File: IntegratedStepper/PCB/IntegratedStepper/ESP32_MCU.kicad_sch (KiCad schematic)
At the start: 0 parts

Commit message: Update Integrated Stepper PCB with ESP sch and CAN sch
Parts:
- added C12, C19: 10uF, Capacitor_SMD:C_0603_1608Metric, symbol Device:C
- added C13, C14, C18: 0.1uF, Capacitor_SMD:C_0603_1608Metric, symbol Device:C
- added Q1, Q2: SS8050-G, SOT95P240X115-3N, symbol SamacSys_Parts:SS8050-G
- added R10: 22.1k, Resistor_SMD:R_0603_1608Metric, symbol Device:R_US
- added R11: 10, Resistor_SMD:R_0603_1608Metric, symbol Device:R_US
- added R12, R15, R16, R17, R18: 2k, Resistor_SMD:R_0603_1608Metric, symbol Device:R_US
- added R13, R14, R6: 10k, Resistor_SMD:R_0603_1608Metric, symbol Device:R_US
- added R9: 47.5k, Resistor_SMD:R_0603_1608Metric, symbol Device:R_US
- added U1: ESP32-WROOM-32E, RF_Module:ESP32-WROOM-32D, symbol RF_Module:ESP32-WROOM-32E
- added U3: CP2102N-Axx-xQFN28, Package_DFN_QFN:QFN-28-1EP_5x5mm_P0.5mm_EP3.35x3.35mm, symbol Interface_USB:CP2102N-Axx-xQFN28
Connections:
- new net: R12.1, U3.9 (~{RST})
- new net: Q2.1 (B), R14.2
- new net: R10.1, R9.1, U3.8 (VBUS)
- new net: Q1.1 (B), R13.2
- new net: R11.2, U1.35 (TXD0/IO1)
- new net 3V3_VCC: C12.1, C13.1, C18.1, C19.1, R12.2, R15.2, R17.1, R18.1, R6.1, U1.2 (VDD), U3.6 (VDD), U3.7 (VREGIN)
- new net CAN_RX: U1.28 (IO17)
- new net CAN_TX: U1.27 (IO16)
- new net DTR: Q2.2 (E), R13.1, U3.28 (~{DTR})
- new net EN: C14.1, Q1.3 (C), R6.2, U1.3 (EN)
- new net EN1: R17.2, U1.31 (IO19)
- new net EN3: R18.2, U1.37 (IO23)
- new net GND: C12.2, C13.2, C14.2, C18.2, C19.2, R16.1, R9.2, U1.1 (GND), U1.15 (GND), U1.38 (GND), U1.39 (GND), U3.29 (GND), U3.3 (GND)
- new net IN1: U1.10 (IO25)
- new net IN2: U1.11 (IO26)
- new net IN3: U1.9 (IO33)
- new net IN4: U1.8 (IO32)
- new net IO0: Q2.3 (C), U1.25 (IO0)
- new net M_CS0: R15.1, U1.23 (IO15)
- new net M_MISO: R16.2, U1.14 (IO12)
- new net M_MOSI: U1.16 (IO13)
- new net M_SCLK: U1.13 (IO14)
- new net RTS: Q1.2 (E), R14.1, U3.24 (~{RTS})
- new net RX: U1.34 (RXD0/IO3), U3.26 (TXD)
- new net TX: R11.1, U3.25 (RXD)
- new net USB_D+: U3.4 (D+)
- new net USB_D-: U3.5 (D-)
- new net VUSB: R10.2

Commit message: Update Integrated Stepper with inital PCB
This is going to be so hard :(
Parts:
- added C20, C21: 0.1uF, Capacitor_SMD:C_0603_1608Metric_Pad1.08x0.95mm_HandSolder, symbol Device:C
- added EN1, IO0: PTS815_SJG_250_SMTR_LFS, SamacSys_Parts:PTS815SJM250SMTRLFS, symbol SamacSys_Parts:PTS815_SJG_250_SMTR_LFS
- added R22: 500, Resistor_SMD:R_0603_1608Metric, symbol Device:R_US
- added V3v3: LED, LED_SMD:LED_0603_1608Metric, symbol Device:LED
- C13, C14, C18: footprint Capacitor_SMD:C_0603_1608Metric -> Capacitor_SMD:C_0603_1608Metric_Pad1.08x0.95mm_HandSolder
- R17, R18: now not fitted
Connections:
- net 3V3_VCC: now also V3v3.2 (A)
- net EN: now also C21.1, EN1.1 (COM_1)
- net GND: now also C20.2, C21.2, EN1.3 (NO_1), IO0.3 (NO_1), R22.1
- net IO0: now also C20.1, IO0.1 (COM_1)
- net ENC+: now reaches U1.12 (IO27)
- net ENC_IND: now reaches U1.24 (IO2)
- net ENC-: now reaches U1.30 (IO18)
- net I2C_SDA: now reaches U1.33 (IO21)
- net I2C_SCL: now reaches U1.36 (IO22)
- net M_FAULT: now reaches U1.7 (IO35)
- new net: R22.2, V3v3.1 (K)

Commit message: Add final layout + 3D models
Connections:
- net EN1: now also R18.2, U1.37 (IO23); no longer R17.2, U1.31 (IO19)
- net EN3: now also R17.2, U1.31 (IO19); no longer R18.2, U1.37 (IO23)
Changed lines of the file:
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@@
 		)
 	)
-	(label "EN2"
+	(label "EN4"
 		(at 170.18 88.9 0)
+		(fields_autoplaced yes)
 		(effects
 			(font
@@
 		)
 	)
-	(label "EN4"
+	(label "EN2"
 		(at 170.18 93.98 0)
+		(fields_autoplaced yes)
 		(effects
 			(font
@@
 		)
 	)
-	(label "EN3"
+	(label "EN1"
 		(at 170.18 91.44 0)
+		(fields_autoplaced yes)
 		(effects
 			(font
@@
 		)
 	)
-	(label "EN1"
+	(label "EN3"
 		(at 170.18 86.36 0)
+		(fields_autoplaced yes)
 		(effects
 			(font

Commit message: add changes for instock parts
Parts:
- EN1, IO0: LCSC (none) -> C411883; LCSC Part (none) -> C411883; LCSC Part Number (none) -> C411883
- Q1: LCSC Part (none) -> C916392; LCSC Part Number (none) -> C916392
- Q2: LCSC (none) -> C916392; LCSC Part (none) -> C916392; LCSC Part Number (none) -> C916392
- R10: LCSC (none) -> C2989573; LCSC Part (none) -> C2989573; LCSC Part Number (none) -> C2989573
- R11: LCSC (none) -> C177687; LCSC Part (none) -> C177687; LCSC Part Number (none) -> C177687
- R12, R15, R16, R17, R18: LCSC (none) -> C217936; LCSC Part (none) -> C217936; LCSC Part Number (none) -> C217936
- R13, R14, R6: LCSC (none) -> C469659; LCSC Part (none) -> C469659; LCSC Part Number (none) -> C469659
- R22: LCSC (none) -> C2989147; LCSC Part (none) -> C2989147; LCSC Part Number (none) -> C2989147
- R9: LCSC (none) -> C319608; LCSC Part (none) -> C319608; LCSC Part Number (none) -> C319608
- U1: LCSC (none) -> C701341; LCSC Part (none) -> C701341; LCSC Part Number (none) -> C701341
- U3: LCSC (none) -> C964632; LCSC Part (none) -> C964632; LCSC Part Number (none) -> C964632

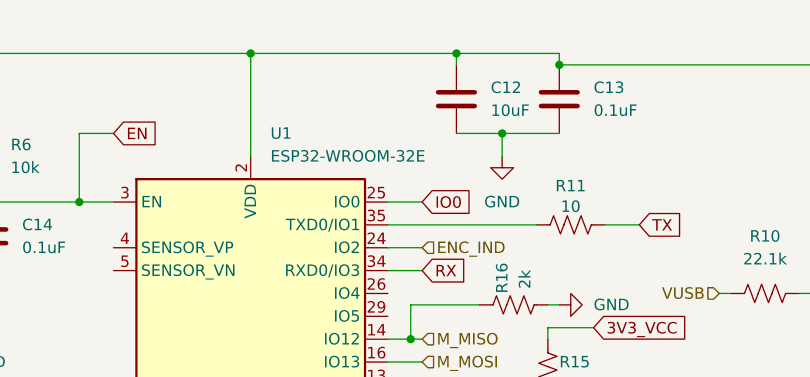
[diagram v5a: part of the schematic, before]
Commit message: update with more in stock parts
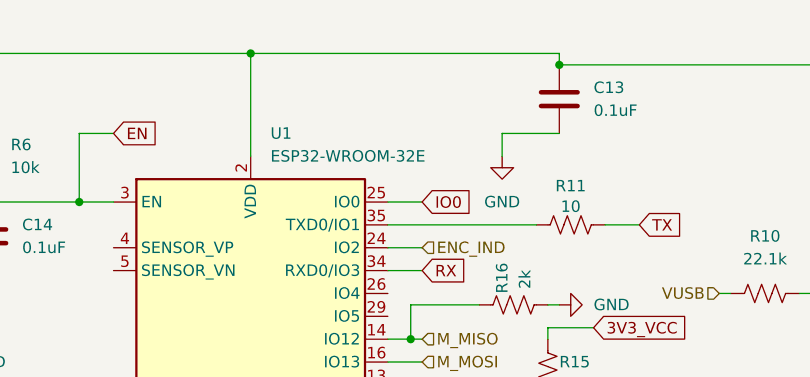
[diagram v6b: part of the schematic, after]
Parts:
- removed C12: 10uF, Capacitor_SMD:C_0603_1608Metric, symbol Device:C
- C13, C14, C18, C20, C21: footprint Capacitor_SMD:C_0603_1608Metric_Pad1.08x0.95mm_HandSolder -> Capacitor_SMD:C_0603_1608Metric; LCSC (none) -> C2929200; LCSC Part (none) -> C2929200; LCSC Part Number (none) -> C2929200
- C19: LCSC (none) -> C96446; LCSC Part (none) -> C96446; LCSC Part Number (none) -> C96446
- V3v3: LCSC (none) -> C965804; LCSC Part (none) -> C965804; LCSC Part Number (none) -> C965804
